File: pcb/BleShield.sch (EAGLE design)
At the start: 29 parts, among them U1 ARDUINO_SHIELDNOHOLES, Y1 32.768KHz, 10 PPM

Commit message: Swap out programming headers to 1.27mm, to match module pitch (only a master will use these anyway?)
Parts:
- removed JP3: M09, SparkFun:M09
- added JP1, JP4: (no value), SparkFun:M051.27MM
- JP2: device SparkFun:M05PTH -> SparkFun:M041.27MM
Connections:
- net 3.3V: now also JP2.3; no longer JP3.3
- net GND: now also JP1.1; no longer JP3.1
- net N$1: now also JP4.1; no longer JP3.5
- net N$12: now also JP4.4; no longer JP3.8
- net N$13: now also JP4.3; no longer JP3.7
- net N$14: now also JP4.2; no longer JP3.6
- net N$15: now also JP1.2; no longer JP2.2
- net N$16: now also JP1.3; no longer JP2.3
- net N$18: now also JP1.4; no longer JP2.4
- net N$8: now also JP4.5; no longer JP3.9
- net N$9: now also JP1.5; no longer JP2.5
- net RX: now also JP2.2; no longer JP3.2
- net TX: now also JP2.4; no longer JP3.4
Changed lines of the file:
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@@
 <part name="R12" library="SparkFun" deviceset="RESISTOR" device="0805-RES" value="DNP"/>
 <part name="R13" library="SparkFun" deviceset="RESISTOR" device="0805-RES" value="DNP"/>
-<part name="JP2" library="SparkFun" deviceset="M05" device="PTH"/>
-<part name="JP3" library="SparkFun" deviceset="M09" device=""/>
+<part name="JP1" library="SparkFun" deviceset="M05" device="1.27MM"/>
+<part name="JP2" library="SparkFun" deviceset="M04" device="1.27MM"/>
+<part name="JP4" library="SparkFun" deviceset="M05" device="1.27MM"/>
 </parts>
 <sheets>
@@
 <instance part="R12" gate="G$1" x="58.42" y="109.22"/>
 <instance part="R13" gate="G$1" x="58.42" y="106.68"/>
-<instance part="JP2" gate="G$1" x="213.36" y="111.76" rot="R180"/>
-<instance part="JP3" gate="G$1" x="157.48" y="53.34" rot="R90"/>
+<instance part="JP1" gate="G$1" x="213.36" y="111.76" rot="R180"/>
+<instance part="JP2" gate="G$1" x="165.1" y="58.42" rot="R90"/>
+<instance part="JP4" gate="G$1" x="152.4" y="55.88" rot="R90"/>
 </instances>
 <busses>
@@
 <junction x="165.1" y="81.28"/>
 <wire x1="165.1" y1="81.28" x2="165.1" y2="63.5" width="0.1524" layer="91"/>
-<pinref part="JP3" gate="G$1" pin="2"/>
+<pinref part="JP2" gate="G$1" pin="2"/>
 </segment>
 <segment>
@@
 <junction x="160.02" y="86.36"/>
 <wire x1="160.02" y1="86.36" x2="160.02" y2="63.5" width="0.1524" layer="91"/>
-<pinref part="JP3" gate="G$1" pin="4"/>
+<pinref part="JP2" gate="G$1" pin="4"/>
 </segment>
 <segment>
@@
 <junction x="162.56" y="83.82"/>
 <wire x1="162.56" y1="83.82" x2="162.56" y2="63.5" width="0.1524" layer="91"/>
-<pinref part="JP3" gate="G$1" pin="3"/>
+<pinref part="JP2" gate="G$1" pin="3"/>
 </segment>
 </net>
@@
 <wire x1="205.74" y1="116.84" x2="187.96" y2="116.84" width="0.1524" layer="91"/>
 <junction x="187.96" y="116.84"/>
-<pinref part="JP2" gate="G$1" pin="1"/>
+<pinref part="JP1" gate="G$1" pin="1"/>
 </segment>
 <segment>
@@
 <junction x="167.64" y="68.58"/>
 <wire x1="167.64" y1="68.58" x2="167.64" y2="63.5" width="0.1524" layer="91"/>
-<pinref part="JP3" gate="G$1" pin="1"/>
+<pinref part="JP2" gate="G$1" pin="1"/>
 </segment>
 <segment>
@@
 <wire x1="157.48" y1="73.66" x2="157.48" y2="63.5" width="0.1524" layer="91"/>
 <junction x="157.48" y="73.66"/>
-<pinref part="JP3" gate="G$1" pin="5"/>
+<pinref part="JP4" gate="G$1" pin="1"/>
 </segment>
 </net>
@@
 <wire x1="200.66" y1="106.68" x2="205.74" y2="106.68" width="0.1524" layer="91"/>
 <junction x="200.66" y="106.68"/>
-<pinref part="JP2" gate="G$1" pin="5"/>
+<pinref part="JP1" gate="G$1" pin="5"/>
 </segment>
 </net>
@@
 <pinref part="U$1" gate="G$1" pin="P2.2"/>
 <wire x1="147.32" y1="88.9" x2="147.32" y2="63.5" width="0.1524" layer="91"/>
-<pinref part="JP3" gate="G$1" pin="9"/>
+<pinref part="JP4" gate="G$1" pin="5"/>
 </segment>
 </net>
@@
 <pinref part="U$1" gate="G$1" pin="P2.1"/>
 <wire x1="149.86" y1="63.5" x2="149.86" y2="88.9" width="0.1524" layer="91"/>
-<pinref part="JP3" gate="G$1" pin="8"/>
+<pinref part="JP4" gate="G$1" pin="4"/>
 </segment>
 </net>
@@
 <pinref part="U$1" gate="G$1" pin="P1.4/CT"/>
 <wire x1="152.4" y1="88.9" x2="152.4" y2="63.5" width="0.1524" layer="91"/>
-<pinref part="JP3" gate="G$1" pin="7"/>
+<pinref part="JP4" gate="G$1" pin="3"/>
 </segment>
 </net>
@@
 <pinref part="U$1" gate="G$1" pin="P1.5/RT"/>
 <wire x1="154.94" y1="63.5" x2="154.94" y2="88.9" width="0.1524" layer="91"/>
-<pinref part="JP3" gate="G$1" pin="6"/>
+<pinref part="JP4" gate="G$1" pin="2"/>
 </segment>
 </net>
@@
 <pinref part="U$1" gate="G$1" pin="P0.4"/>
 <wire x1="175.26" y1="114.3" x2="205.74" y2="114.3" width="0.1524" layer="91"/>
-<pinref part="JP2" gate="G$1" pin="2"/>
+<pinref part="JP1" gate="G$1" pin="2"/>
 </segment>
 </net>
@@
 <pinref part="U$1" gate="G$1" pin="P0.5"/>
 <wire x1="205.74" y1="111.76" x2="175.26" y2="111.76" width="0.1524" layer="91"/>
-<pinref part="JP2" gate="G$1" pin="3"/>
+<pinref part="JP1" gate="G$1" pin="3"/>
 </segment>
 </net>
@@
 <pinref part="U$1" gate="G$1" pin="P0.6"/>
 <wire x1="175.26" y1="109.22" x2="205.74" y2="109.22" width="0.1524" layer="91"/>
-<pinref part="JP2" gate="G$1" pin="4"/>
-</segment>
-</net>
+<pinref part="JP1" gate="G$1" pin="4"/>
+</segment>
+</net>

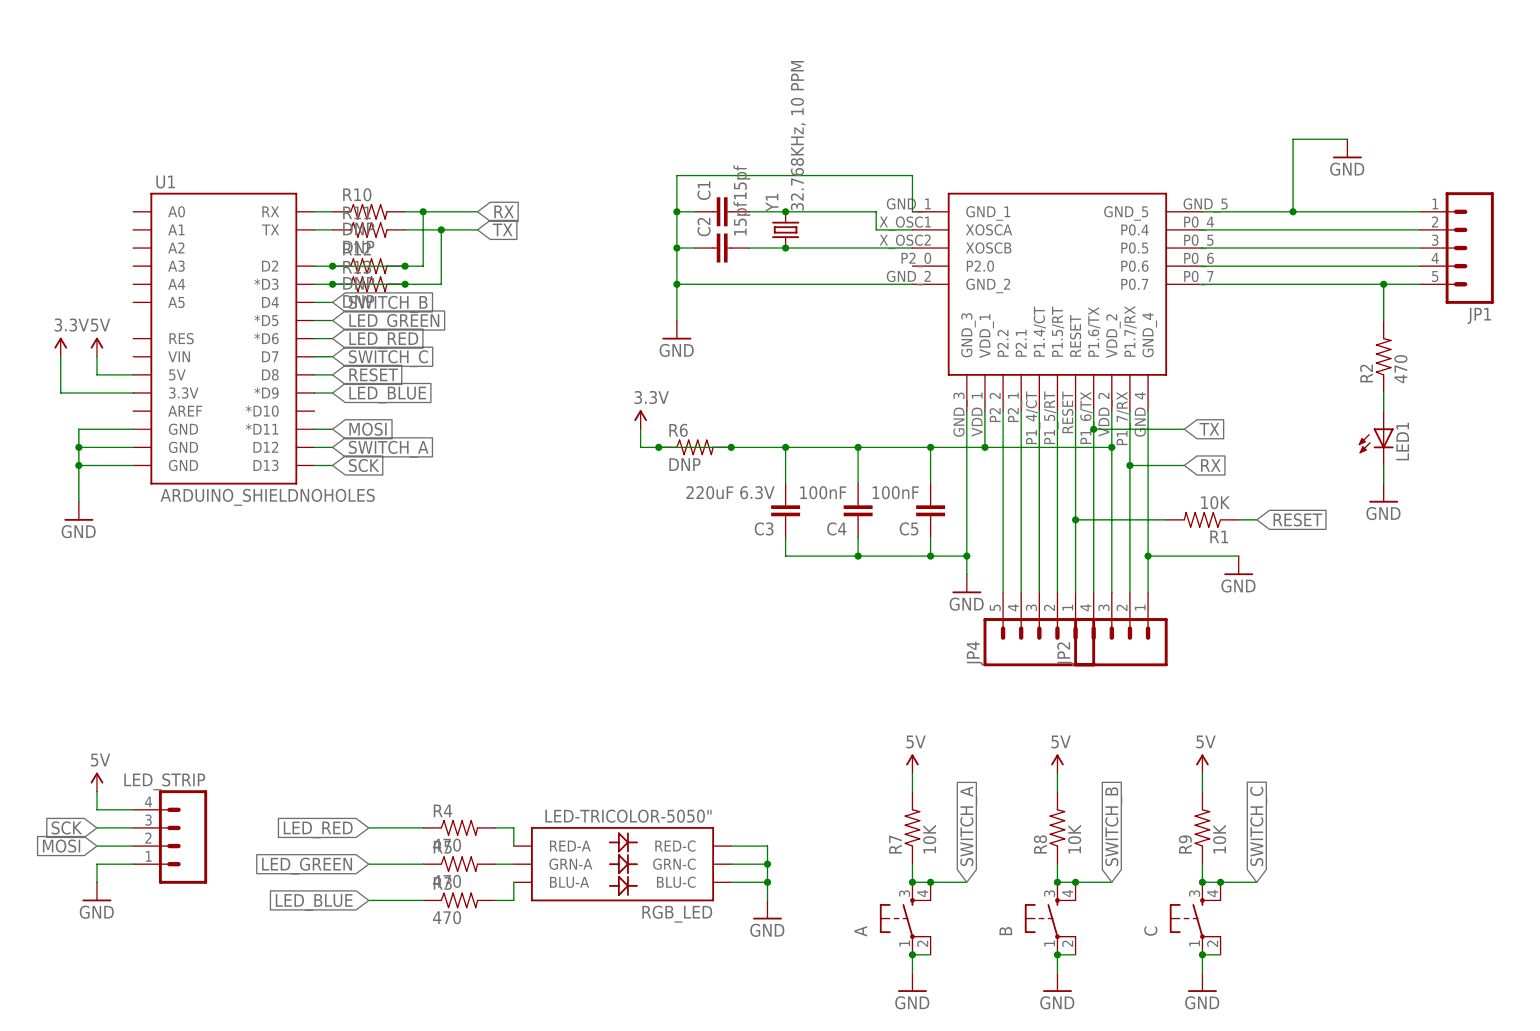
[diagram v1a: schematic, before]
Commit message: Knocked out everything except crystal pad and RX/TX doublecheck.
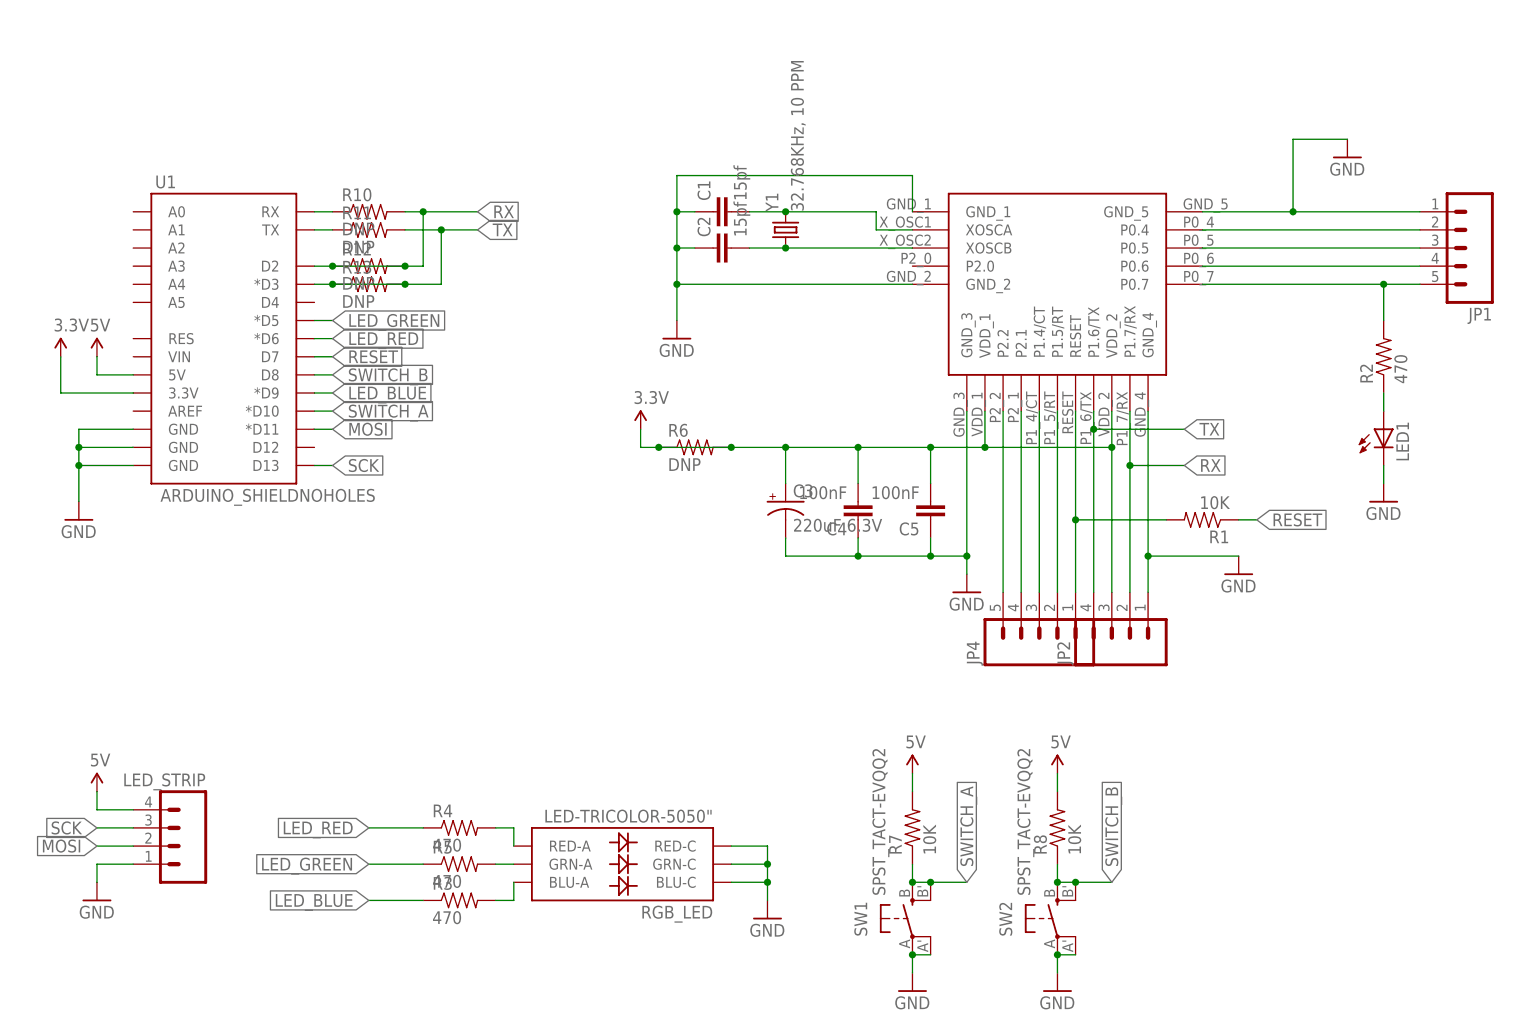
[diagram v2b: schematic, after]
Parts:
- removed A, B, C: (no value), SparkFun:TAC_SWITCHSMD
- removed R9: 10K, SparkFun:RESISTOR0805-RES
- added SW1, SW2: SPST_TACT-EVQQ2, adafruit:SPST_TACT-EVQQ2
- C3: device SparkFun:CAP0805 -> rcl:CPOL-USC/6032-28R
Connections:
- removed net SWITCH_C: C.3, C.4, R9.1, U1.D7
- net 3.3V: now also C3.+; no longer C3.2
- net 5V: no longer R9.2
- net GND: now also C3.-, SW1.P, SW1.P1, SW2.P, SW2.P1; no longer A.1, A.2, B.1, B.2, C.1, C.2, C3.1
- net RESET: now also U1.D7; no longer U1.D8
- net SWITCH_A: now also SW1.S, SW1.S1, U1.*D10; no longer A.3, A.4, U1.D12
- net SWITCH_B: now also SW2.S, SW2.S1, U1.D8; no longer B.3, B.4, U1.D4
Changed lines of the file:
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@@
 <part name="C1" library="SparkFun" deviceset="CAP" device="0805" value="15pf"/>
 <part name="C2" library="SparkFun" deviceset="CAP" device="0805" value="15pf"/>
-<part name="C3" library="SparkFun" deviceset="CAP" device="0805" value="220uF 6.3V"/>
 <part name="C4" library="SparkFun" deviceset="CAP" device="0805" value="100nF"/>
 <part name="C5" library="SparkFun" deviceset="CAP" device="0805" value="100nF"/>
@@
 <part name="R7" library="SparkFun" deviceset="RESISTOR" device="0805-RES" value="10K"/>
 <part name="GND8" library="SparkFun" deviceset="GND" device=""/>
-<part name="B" library="SparkFun" deviceset="TAC_SWITCH" device="SMD"/>
 <part name="U$5" library="SparkFun" deviceset="5V" device=""/>
 <part name="R8" library="SparkFun" deviceset="RESISTOR" device="0805-RES" value="10K"/>
 <part name="GND9" library="SparkFun" deviceset="GND" device=""/>
-<part name="C" library="SparkFun" deviceset="TAC_SWITCH" device="SMD"/>
-<part name="U$6" library="SparkFun" deviceset="5V" device=""/>
-<part name="R9" library="SparkFun" deviceset="RESISTOR" device="0805-RES" value="10K"/>
-<part name="GND10" library="SparkFun" deviceset="GND" device=""/>
 <part name="RGB_LED" library="blinkiverse" deviceset="LED-TRICOLOR-5050" device="&quot;"/>
 <part name="Y1" library="blinkiverse" deviceset="CRYSTAL" device="" value="32.768KHz, 10 PPM"/>
-<part name="A" library="SparkFun" deviceset="TAC_SWITCH" device="SMD"/>
 <part name="LED1" library="adafruit" deviceset="LED" device="CHIPLED_0805"/>
 <part name="R2" library="SparkFun" deviceset="RESISTOR" device="0805-RES" value="470"/>
@@
 <part name="JP2" library="SparkFun" deviceset="M04" device="1.27MM"/>
 <part name="JP4" library="SparkFun" deviceset="M05" device="1.27MM"/>
+<part name="C3" library="rcl" deviceset="CPOL-US" device="C/6032-28R" value="220uF 6.3V"/>
+<part name="SW1" library="adafruit" deviceset="SPST_TACT" device="-EVQQ2"/>
+<part name="SW2" library="adafruit" deviceset="SPST_TACT" device="-EVQQ2"/>
 </parts>
 <sheets>
@@
 <instance part="C1" gate="G$1" x="109.22" y="116.84" rot="R90"/>
 <instance part="C2" gate="G$1" x="109.22" y="111.76" rot="R90"/>
-<instance part="C3" gate="G$1" x="116.84" y="76.2" rot="R180"/>
 <instance part="C4" gate="G$1" x="127" y="76.2" rot="R180"/>
 <instance part="C5" gate="G$1" x="137.16" y="76.2" rot="R180"/>
@@
 <instance part="R7" gate="G$1" x="134.62" y="30.48" rot="R90"/>
 <instance part="GND8" gate="1" x="134.62" y="7.62"/>
-<instance part="B" gate="S" x="154.94" y="17.78" rot="R90"/>
 <instance part="U$5" gate="G$1" x="154.94" y="38.1"/>
 <instance part="R8" gate="G$1" x="154.94" y="30.48" rot="R90"/>
 <instance part="GND9" gate="1" x="154.94" y="7.62"/>
-<instance part="C" gate="S" x="175.26" y="17.78" rot="R90"/>
-<instance part="U$6" gate="G$1" x="175.26" y="38.1"/>
-<instance part="R9" gate="G$1" x="175.26" y="30.48" rot="R90"/>
-<instance part="GND10" gate="1" x="175.26" y="7.62"/>
 <instance part="RGB_LED" gate="G$1" x="93.98" y="25.4" rot="R180"/>
 <instance part="Y1" gate="G$1" x="116.84" y="114.3" rot="R90"/>
-<instance part="A" gate="S" x="134.62" y="17.78" rot="R90"/>
 <instance part="LED1" gate="G$1" x="200.66" y="86.36"/>
 <instance part="R2" gate="G$1" x="200.66" y="96.52" rot="R90"/>
@@
 <instance part="JP2" gate="G$1" x="165.1" y="58.42" rot="R90"/>
 <instance part="JP4" gate="G$1" x="152.4" y="55.88" rot="R90"/>
+<instance part="C3" gate="G$1" x="116.84" y="76.2"/>
+<instance part="SW1" gate="G$1" x="134.62" y="17.78"/>
+<instance part="SW2" gate="G$1" x="154.94" y="17.78"/>
 </instances>
 <busses>
@@
 <wire x1="162.56" y1="83.82" x2="162.56" y2="88.9" width="0.1524" layer="91"/>
 <junction x="144.78" y="83.82"/>
-<pinref part="C3" gate="G$1" pin="2"/>
 <wire x1="116.84" y1="78.74" x2="116.84" y2="83.82" width="0.1524" layer="91"/>
 <pinref part="C4" gate="G$1" pin="2"/>
@@
 <wire x1="162.56" y1="83.82" x2="162.56" y2="63.5" width="0.1524" layer="91"/>
 <pinref part="JP2" gate="G$1" pin="3"/>
+<pinref part="C3" gate="G$1" pin="+"/>
 </segment>
 </net>
@@
 <wire x1="137.16" y1="68.58" x2="127" y2="68.58" width="0.1524" layer="91"/>
 <wire x1="127" y1="71.12" x2="127" y2="68.58" width="0.1524" layer="91"/>
-<pinref part="C3" gate="G$1" pin="1"/>
 <wire x1="127" y1="68.58" x2="116.84" y2="68.58" width="0.1524" layer="91"/>
 <wire x1="116.84" y1="68.58" x2="116.84" y2="71.12" width="0.1524" layer="91"/>
@@
 <junction x="127" y="68.58"/>
 <junction x="142.24" y="68.58"/>
+<pinref part="C3" gate="G$1" pin="-"/>
 </segment>
 <segment>
@@
 <pinref part="GND8" gate="1" pin="GND"/>
 <wire x1="134.62" y1="12.7" x2="134.62" y2="10.16" width="0.1524" layer="91"/>
-<pinref part="A" gate="S" pin="1"/>
 <junction x="134.62" y="12.7"/>
-<pinref part="A" gate="S" pin="2"/>
-</segment>
-<segment>
-<pinref part="B" gate="S" pin="2"/>
-<pinref part="B" gate="S" pin="1"/>
+<pinref part="SW1" gate="G$1" pin="P"/>
+<pinref part="SW1" gate="G$1" pin="P1"/>
+</segment>
+<segment>
 <wire x1="157.48" y1="12.7" x2="154.94" y2="12.7" width="0.1524" layer="91"/>
 <pinref part="GND9" gate="1" pin="GND"/>
 <wire x1="154.94" y1="12.7" x2="154.94" y2="10.16" width="0.1524" layer="91"/>
 <junction x="154.94" y="12.7"/>
-</segment>
-<segment>
-<pinref part="C" gate="S" pin="2"/>
-<pinref part="C" gate="S" pin="1"/>
-<wire x1="177.8" y1="12.7" x2="175.26" y2="12.7" width="0.1524" layer="91"/>
-<pinref part="GND10" gate="1" pin="GND"/>
-<wire x1="175.26" y1="12.7" x2="175.26" y2="10.16" width="0.1524" layer="91"/>
-<junction x="175.26" y="12.7"/>
+<pinref part="SW2" gate="G$1" pin="P"/>
+<pinref part="SW2" gate="G$1" pin="P1"/>
 </segment>
 <segment>
@@
 </segment>
 <segment>
-<pinref part="U1" gate="G$1" pin="D8"/>
-<wire x1="50.8" y1="93.98" x2="53.34" y2="93.98" width="0.1524" layer="91"/>
-<label x="53.34" y="93.98" size="1.778" layer="95" xref="yes"/>
+<label x="53.34" y="96.52" size="1.778" layer="95" xref="yes"/>
+<pinref part="U1" gate="G$1" pin="D7"/>
+<wire x1="50.8" y1="96.52" x2="53.34" y2="96.52" width="0.1524" layer="91"/>
 </segment>
 </net>
@@
 <wire x1="154.94" y1="38.1" x2="154.94" y2="35.56" width="0.1524" layer="91"/>
 </segment>
-<segment>
-<pinref part="U$6" gate="G$1" pin="5V"/>
-<pinref part="R9" gate="G$1" pin="2"/>
-<wire x1="175.26" y1="38.1" x2="175.26" y2="35.56" width="0.1524" layer="91"/>
-</segment>
 </net>
 <net name="SWITCH_A" class="0">
@@
 <wire x1="134.62" y1="22.86" x2="137.16" y2="22.86" width="0.1524" layer="91"/>
 <label x="142.24" y="22.86" size="1.778" layer="95" rot="R90" xref="yes"/>
-<pinref part="A" gate="S" pin="3"/>
 <junction x="134.62" y="22.86"/>
-<pinref part="A" gate="S" pin="4"/>
 <wire x1="137.16" y1="22.86" x2="142.24" y2="22.86" width="0.1524" layer="91"/>
 <junction x="137.16" y="22.86"/>
-</segment>
-<segment>
-<pinref part="U1" gate="G$1" pin="D12"/>
-<wire x1="50.8" y1="83.82" x2="53.34" y2="83.82" width="0.1524" layer="91"/>
-<label x="53.34" y="83.82" size="1.778" layer="95" xref="yes"/>
+<pinref part="SW1" gate="G$1" pin="S"/>
+<pinref part="SW1" gate="G$1" pin="S1"/>
+</segment>
+<segment>
+<label x="53.34" y="88.9" size="1.778" layer="95" xref="yes"/>
+<pinref part="U1" gate="G$1" pin="*D10"/>
+<wire x1="50.8" y1="88.9" x2="53.34" y2="88.9" width="0.1524" layer="91"/>
 </segment>
 </net>
@@
 <segment>
 <pinref part="R8" gate="G$1" pin="1"/>
-<pinref part="B" gate="S" pin="3"/>
 <wire x1="154.94" y1="25.4" x2="154.94" y2="22.86" width="0.1524" layer="91"/>
-<pinref part="B" gate="S" pin="4"/>
 <wire x1="157.48" y1="22.86" x2="154.94" y2="22.86" width="0.1524" layer="91"/>
 <junction x="154.94" y="22.86"/>
@@
 <wire x1="157.48" y1="22.86" x2="162.56" y2="22.86" width="0.1524" layer="91"/>
 <label x="162.56" y="22.86" size="1.778" layer="95" rot="R90" xref="yes"/>
-</segment>
-<segment>
-<pinref part="U1" gate="G$1" pin="D4"/>
-<wire x1="50.8" y1="104.14" x2="53.34" y2="104.14" width="0.1524" layer="91"/>
-<label x="53.34" y="104.14" size="1.778" layer="95" xref="yes"/>
-</segment>
-</net>
-<net name="SWITCH_C" class="0">
-<segment>
-<pinref part="R9" gate="G$1" pin="1"/>
-<pinref part="C" gate="S" pin="3"/>
-<wire x1="175.26" y1="25.4" x2="175.26" y2="22.86" width="0.1524" layer="91"/>
-<pinref part="C" gate="S" pin="4"/>
-<wire x1="177.8" y1="22.86" x2="175.26" y2="22.86" width="0.1524" layer="91"/>
-<junction x="175.26" y="22.86"/>
-<junction x="177.8" y="22.86"/>
-<wire x1="177.8" y1="22.86" x2="182.88" y2="22.86" width="0.1524" layer="91"/>
-<label x="182.88" y="22.86" size="1.778" layer="95" rot="R90" xref="yes"/>
-</segment>
-<segment>
-<pinref part="U1" gate="G$1" pin="D7"/>
-<wire x1="50.8" y1="96.52" x2="53.34" y2="96.52" width="0.1524" layer="91"/>
-<label x="53.34" y="96.52" size="1.778" layer="95" xref="yes"/>
-</segment>
-</net>
+<pinref part="SW2" gate="G$1" pin="S"/>
+<pinref part="SW2" gate="G$1" pin="S1"/>
+</segment>
+<segment>
+<label x="53.34" y="93.98" size="1.778" layer="95" xref="yes"/>
+<pinref part="U1" gate="G$1" pin="D8"/>
+<wire x1="53.34" y1="93.98" x2="50.8" y2="93.98" width="0.1524" layer="91"/>
+</segment>
+</net>
